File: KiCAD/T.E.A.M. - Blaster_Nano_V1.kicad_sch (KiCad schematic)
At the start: 47 parts, among them J1 USB_C_Receptacle_USB2.0_14P, J2 Conn_01x02, J3 Conn_01x02, J4 Conn_01x02, J5 Conn_01x02, J6 Conn_02x03_Counter_Clockwise, Q1 FS8205A, U1 TP4056-42-ESOP8, U2 DW01A, U3 MT3608, U4 ATMEGA328P-AU, U5 CH340G, U6 DFR0299, Y1 Crystal_GND34, Y2 Crystal_GND34

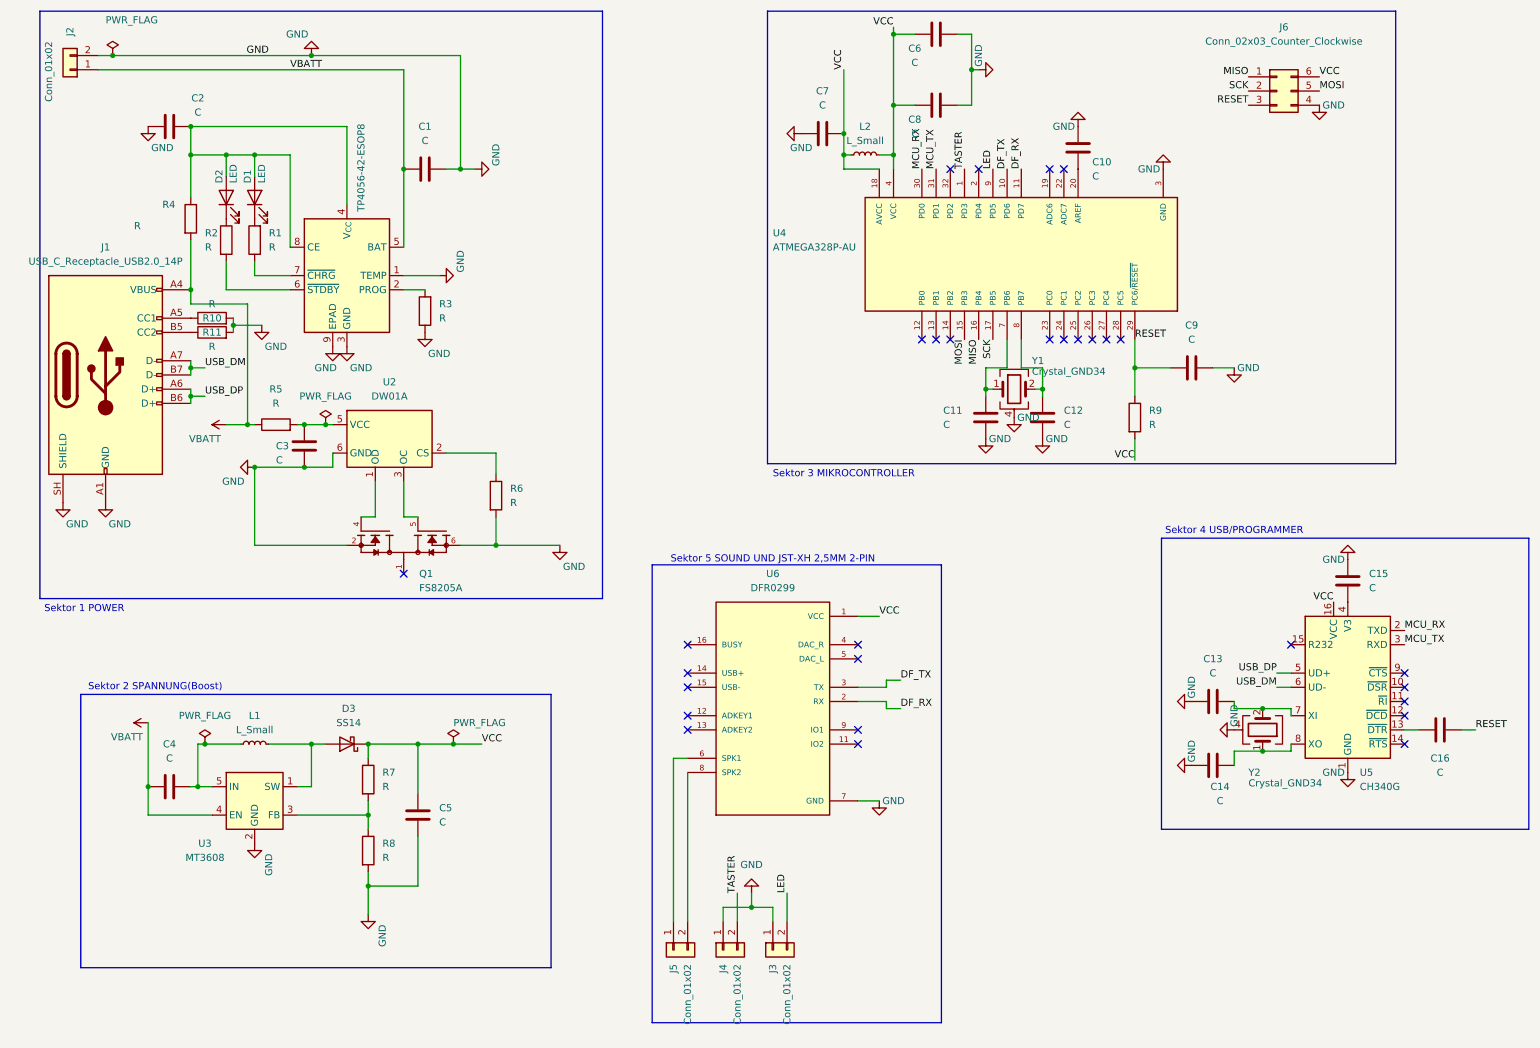
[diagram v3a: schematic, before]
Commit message: Schaltplan finalisiert: alle Sektoren abgeschlossen
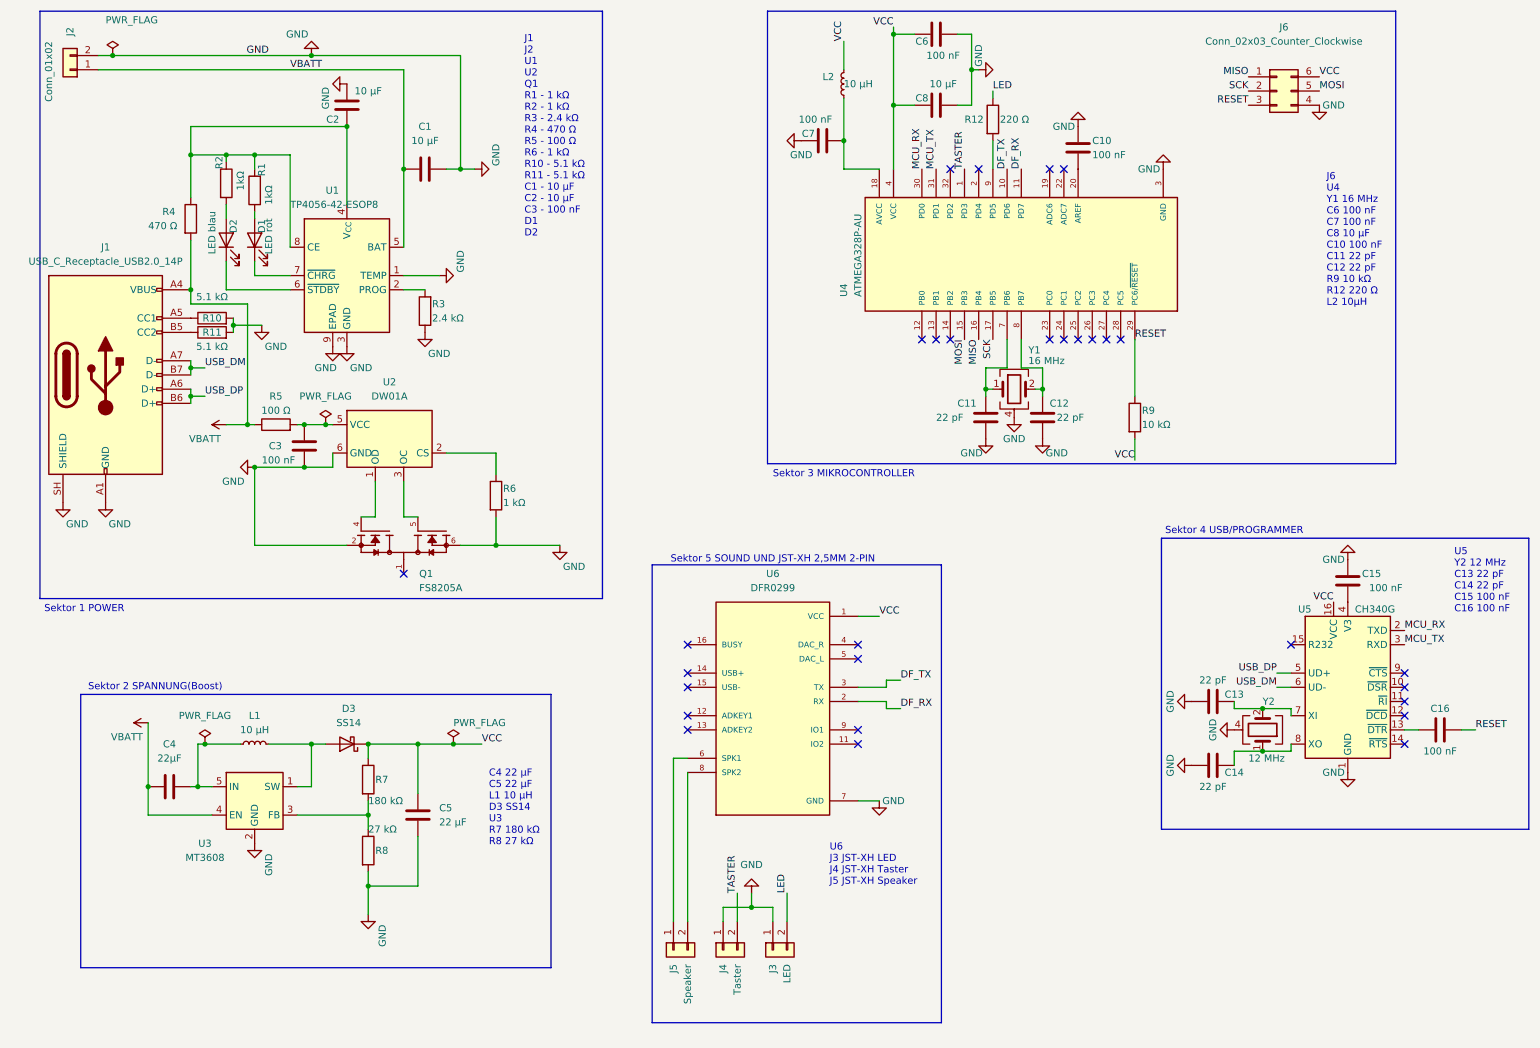
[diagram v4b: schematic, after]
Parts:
- removed C9: C, Capacitor_SMD:C_0402_1005Metric, symbol Device:C
- added R12: 220 Ω, symbol Device:R
- C1, C2, C8: value C -> 10 µF
- C10, C15, C16, C3, C6, C7: value C -> 100 nF
- C11, C12, C13, C14: value C -> 22 pF
- C4: value C -> 22µF
- C5: value C -> 22 µF
- D1: value LED -> LED rot
- D2: value LED -> LED blau
- J3: value Conn_01x02 -> LED
- J4: value Conn_01x02 -> Taster
- J5: value Conn_01x02 -> Speaker
- L1, L2: value L_Small -> 10 µH
- R1, R2: value R -> 1kΩ
- R10, R11: value R -> 5.1 kΩ
- R3: value R -> 2.4 kΩ
- R4: value R -> 470 Ω
- R5: value R -> 100 Ω
- R6: value R -> 1 kΩ
- R7: value R -> 180 kΩ
- R8: value R -> 27 kΩ
- R9: value R -> 10 kΩ
- U1: Funktion (none) -> Laderegler fuer den Akku
- Y1: value Crystal_GND34 -> 16 MHz
- Y2: value Crystal_GND34 -> 12 MHz
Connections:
- net LED: now also R12.1; no longer U4.9 (PD5)
- net VCC: no longer C7.2, L2.1, U4.18 (AVCC)
- net at C2.2, R4.1, U1.4 (V_{CC})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: now also R1.2, R2.1; no longer D1.2 (A), D2.2 (A)
- net at D2.1 (K): now also U1.6 (~{STDBY}); no longer R2.1
- net at R2.2: now also D2.2 (A); no longer U1.6 (~{STDBY})
- net at R1.1: now also D1.2 (A); no longer U1.7 (~{CHRG})
- net at D1.1 (K): now also U1.7 (~{CHRG}); no longer R1.2
- new net: R12.2, U4.9 (PD5)
- new net: C7.2, L2.1, U4.18 (AVCC)
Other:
- note added: "C4 22 µF C5 22 µF L1 10 µH D3 SS14 U3 R7 180 kΩ R8 27 kΩ"
- note added: "J1 J2 U1 U2 Q1 R1 - 1 kΩ R2 - 1 kΩ R3 - 2.4 kΩ R4 - 470 Ω R5 - 100 Ω R6 - 1 kΩ R10 - 5.1 kΩ R11 - 5.1 kΩ C1 - 10 µF C2 - 10 µF C3 - 100 nF D1 D2"
- note added: "J6 U4 Y1 16 MHz C6 100 nF C7 100 nF C8 10 µF C10 100 nF C11 22 pF C12 22 pF R9 10 kΩ R12 220 Ω L2 10µH"
- note added: "U5 Y2 12 MHz C13 22 pF C14 22 pF C15 100 nF C16 100 nF"
- note added: "U6 J3 JST-XH LED J4 JST-XH Taster J5 JST-XH Speaker"
- moved on the sheet: C2, C7, D1, D2, L2, R1, R2

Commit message: Sektor 1: Placement und Routing abgeschlossen
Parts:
- J2: value Conn_01x02 -> Akku
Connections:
- net VBATT: no longer J1.A4 (VBUS), J1.A9 (VBUS), J1.B4 (VBUS), J1.B9 (VBUS), R4.2
- net CS: now reaches R6.1, U2.2 (CS)
- net VUSB: now reaches C2.2, R1.2, R2.1, R4.1, U1.4 (V_{CC}), U1.8 (CE)
- net LED_STDBY: now reaches D2.2 (A), R2.2
- net STDBY: now reaches D2.1 (K), U1.6 (~{STDBY})
- net LED_CHRG: now reaches D1.2 (A), R1.1
- net VCC_PROT: now reaches C3.1, R5.2, U2.5 (VCC)
- net OD: now reaches Q1.4, U2.1 (OD)
- net OC: now reaches Q1.5, U2.3 (OC)
- net PROG: now reaches R3.2, U1.2 (PROG)
- net CHRG: now reaches D1.1 (K), U1.7 (~{CHRG})
- net CC1: now reaches J1.A5 (CC1), R10.1
- net CC2: now reaches J1.B5 (CC2), R11.1
- new net VBUS: J1.A4 (VBUS), J1.A9 (VBUS), J1.B4 (VBUS), J1.B9 (VBUS), R4.2
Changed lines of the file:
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@@
 	)
 	(junction
-		(at 39.37 62.23)
-		(diameter 0)
-		(color 0 0 0 0)
-	)
-	(junction
 		(at 25.4 20.32)
 		(diameter 0)
@@
 	)
 	(junction
-		(at 49.53 86.36)
-		(diameter 0)
-		(color 0 0 0 0)
-	)
-	(junction
 		(at 87.63 40.64)
 		(diameter 0)
@@
 	)
 	(junction
-		(at 39.37 38.1)
+		(at 60.96 86.36)
 		(diameter 0)
 		(color 0 0 0 0)
 	)
 	(junction
-		(at 165.1 29.21)
+		(at 39.37 38.1)
 		(diameter 0)
 		(color 0 0 0 0)
 	)
 	(junction
-		(at 63.5 86.36)
+		(at 165.1 29.21)
 		(diameter 0)
 		(color 0 0 0 0)
@@
 	(wire
 		(pts
-			(xy 49.53 86.36) (xy 50.8 86.36)
+			(xy 45.72 86.36) (xy 50.8 86.36)
 		)
 		(stroke
@@
 	(wire
 		(pts
-			(xy 63.5 86.36) (xy 64.77 86.36)
-		)
-		(stroke
-			(width 0)
-			(type default)
-		)
-	)
-	(wire
-		(pts
 			(xy 87.63 20.32) (xy 87.63 40.64)
 		)
@@
 	(wire
 		(pts
+			(xy 60.96 86.36) (xy 64.77 86.36)
+		)
+		(stroke
+			(width 0)
+			(type default)
+		)
+	)
+	(wire
+		(pts
 			(xy 60.96 151.13) (xy 60.96 143.51)
 		)
@@
 	(wire
 		(pts
-			(xy 39.37 64.77) (xy 39.37 62.23)
-		)
-		(stroke
-			(width 0)
-			(type default)
-		)
-	)
-	(wire
-		(pts
 			(xy 182.88 26.67) (xy 182.88 27.94)
 		)
@@
 	(wire
 		(pts
-			(xy 49.53 64.77) (xy 49.53 86.36)
-		)
-		(stroke
-			(width 0)
-			(type default)
-		)
-	)
-	(wire
-		(pts
 			(xy 125.73 146.05) (xy 125.73 175.26)
 		)
@@
 	(wire
 		(pts
-			(xy 39.37 64.77) (xy 49.53 64.77)
-		)
-		(stroke
-			(width 0)
-			(type default)
-		)
-	)
-	(wire
-		(pts
 			(xy 71.12 153.67) (xy 71.12 156.21)
 		)
@@
 	(wire
 		(pts
-			(xy 59.69 86.36) (xy 63.5 86.36)
+			(xy 59.69 86.36) (xy 60.96 86.36)
 		)
 		(stroke
@@
 		)
 	)
-	(wire
-		(pts
-			(xy 45.72 86.36) (xy 49.53 86.36)
-		)
-		(stroke
-			(width 0)
-			(type default)
-		)
-	)
 	(label "DF_TX"
 		(at 166.37 132.08 0)
@@
 		)
 	)
+	(label "VCC_PROT"
+		(at 64.77 86.36 90)
+		(effects
+			(font
+				(size 1.27 1.27)
+			)
+			(justify left bottom)
+		)
+	)
 	(label "DF_RX"
 		(at 187.96 40.64 90)
@@
 		)
 	)
+	(label "VUSB"
+		(at 55.88 33.02 0)
+		(effects
+			(font
+				(size 1.27 1.27)
+			)
+			(justify left bottom)
+		)
+	)
+	(label "OD"
+		(at 72.39 99.06 0)
+		(effects
+			(font
+				(size 1.27 1.27)
+			)
+			(justify left bottom)
+		)
+	)
 	(label "USB_DP"
 		(at 41.91 81.28 0)
@@
 		)
 	)
+	(label "STDBY"
+		(at 46.99 62.23 0)
+		(effects
+			(font
+				(size 1.27 1.27)
+			)
+			(justify left bottom)
+		)
+	)
 	(label "USB_DP"
 		(at 233.68 130.81 180)
@@
 		)
 	)
+	(label "CS"
+		(at 88.9 91.44 0)
+		(effects
+			(font
+				(size 1.27 1.27)
+			)
+			(justify left bottom)
+		)
+	)
 	(label "USB_DM"
 		(at 233.68 133.35 180)
@@
 		)
 	)
+	(label "CHRG"
+		(at 50.8 59.69 0)
+		(effects
+			(font
+				(size 1.27 1.27)
+			)
+			(justify left bottom)
+		)
+	)
 	(label "VCC"
 		(at 208.28 92.71 180)
@@
 		)
 	)
+	(label "CC2"
+		(at 39.37 69.85 270)
+		(effects
+			(font
+				(size 1.27 1.27)
+			)
+			(justify right bottom)
+		)
+	)
 	(label "USB_DM"
 		(at 41.91 76.2 0)
@@
 		)
 	)
+	(label "CC1"
+		(at 39.37 67.31 90)
+		(effects
+			(font
+				(size 1.27 1.27)
+			)
+			(justify left bottom)
+		)
+	)
 	(label "DF_TX"
 		(at 185.42 40.64 90)
@@
 		)
 	)
+	(label "VBUS"
+		(at 39.37 59.69 0)
+		(effects
+			(font
+				(size 1.27 1.27)
+			)
+			(justify left bottom)
+		)
+	)
+	(label "LED_STDBY"
+		(at 45.72 48.26 90)
+		(effects
+			(font
+				(size 1.27 1.27)
+			)
+			(justify left bottom)
+		)
+	)
+	(label "PROG"
+		(at 77.47 62.23 0)
+		(effects
+			(font
+				(size 1.27 1.27)
+			)
+			(justify left bottom)
+		)
+	)
 	(label "RESET"
 		(at 269.24 140.97 0)
@@
 		)
 	)
+	(label "OC"
+		(at 77.47 100.33 0)
+		(effects
+			(font
+				(size 1.27 1.27)
+			)
+			(justify left bottom)
+		)
+	)
 	(label "RESET"
 		(at 208.28 71.12 0)
@@
 		)
 	)
+	(label "LED_CHRG"
+		(at 50.8 49.53 90)
+		(effects
+			(font
+				(size 1.27 1.27)
+			)
+			(justify left bottom)
+		)
+	)
 	(symbol
 		(lib_id "Device:R")
@@
 	(symbol
 		(lib_id "power:PWR_FLAG")
-		(at 63.5 86.36 0)
+		(at 60.96 86.36 0)
 		(unit 1)
 		(body_style 1)
@@
 		(in_pos_files yes)
 		(dnp no)
-		(fields_autoplaced yes)
 		(property "Reference" "#FLG1"
-			(at 63.5 84.455 0)
+			(at 60.96 84.455 0)
 			(hide yes)
 			(show_name no)
@@
 		)
 		(property "Value" "PWR_FLAG"
-			(at 63.5 81.28 0)
+			(at 59.69 78.74 90)
 			(show_name no)
 			(do_not_autoplace no)
@@
 		)
 		(property "Footprint" ""
-			(at 63.5 86.36 0)
+			(at 60.96 86.36 0)
 			(hide yes)
 			(show_name no)
@@
 		)
 		(property "Datasheet" ""
-			(at 63.5 86.36 0)
+			(at 60.96 86.36 0)
 			(hide yes)
 			(show_name no)
@@
 		)
 		(property "Description" "Special symbol for telling ERC where power comes from"
-			(at 63.5 86.36 0)
+			(at 60.96 86.36 0)
 			(hide yes)
 			(show_name no)
@@
 			)
 		)
-		(property "Value" "Conn_01x02"
+		(property "Value" "Akku"
 			(at 13.97 17.78 90)
 			(show_name no)
@@
 		)
 		(property "Value" "5.1 kΩ"
-			(at 43.18 63.5 90)
+			(at 43.18 64.77 90)
 			(show_name no)
 			(do_not_autoplace no)
